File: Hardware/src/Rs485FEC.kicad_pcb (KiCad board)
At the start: 2 copper layers, 24 x 27.9 mm, 19 parts, among them J1 B3B-XH-A, P1 105444-0001, Q1 DMP3099L-13, U1 FT232RL, U2 SP485E

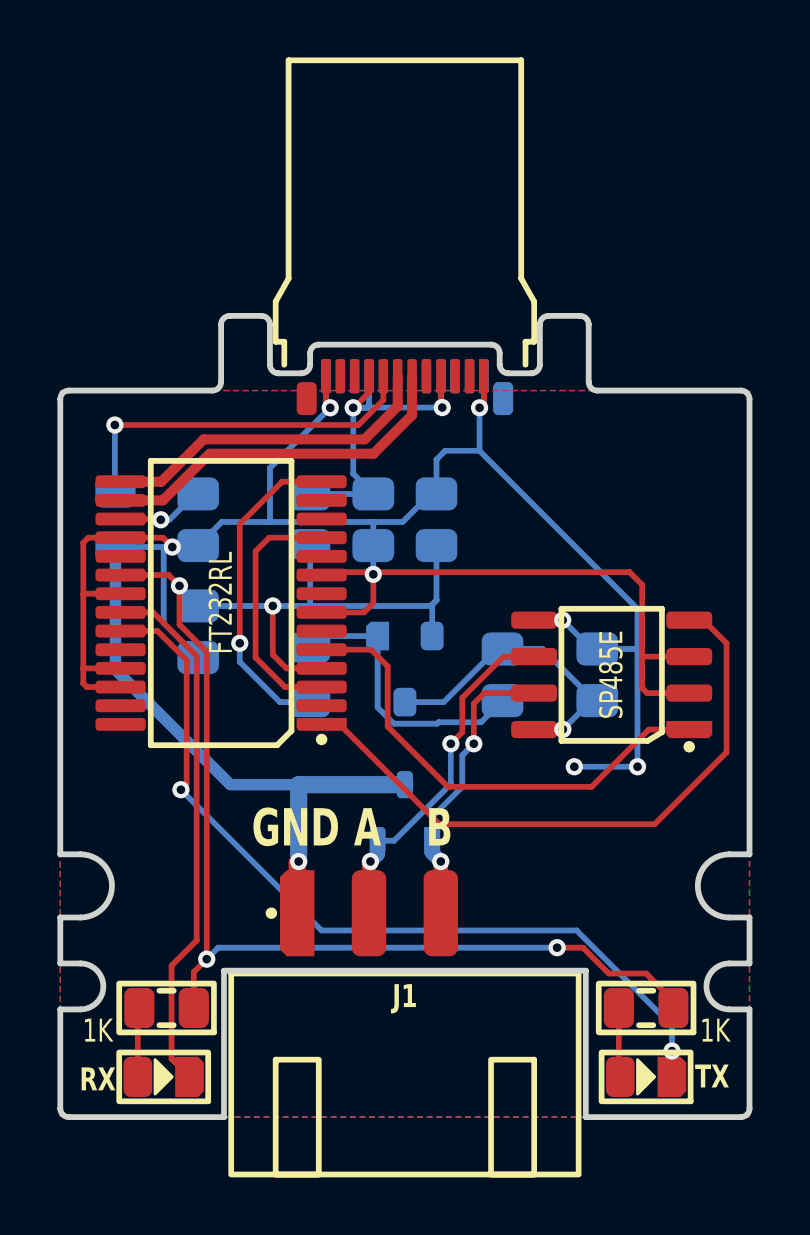
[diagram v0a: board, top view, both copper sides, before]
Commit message: Added RTS/CTS loopback
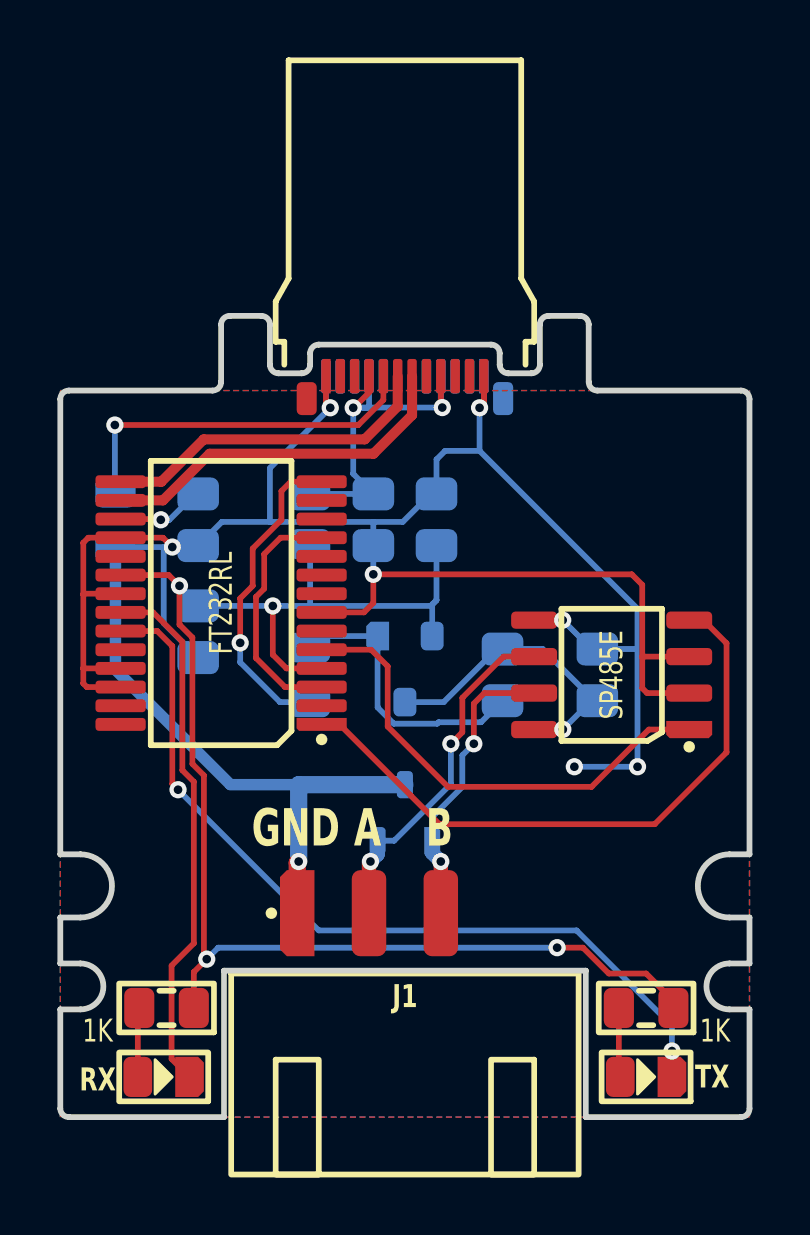
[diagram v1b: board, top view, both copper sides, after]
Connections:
- U1 pad 9: GND -> (no net)
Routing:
- net GND: track 106.9 -> 105.1 mm
